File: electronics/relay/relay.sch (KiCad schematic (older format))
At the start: 14 parts, among them J1 Conn_01x01_Female, J2 Conn_01x01_Female, J3 Conn_01x01_Female, J4 Conn_01x01_Female, J5 Conn_01x01_Female, J6 Conn_01x01_Female, J7 Conn_01x01_Female, J8 Conn_01x01_Female, J9 Conn_01x01_Female, K1 SANYOU_SRD_Form_C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

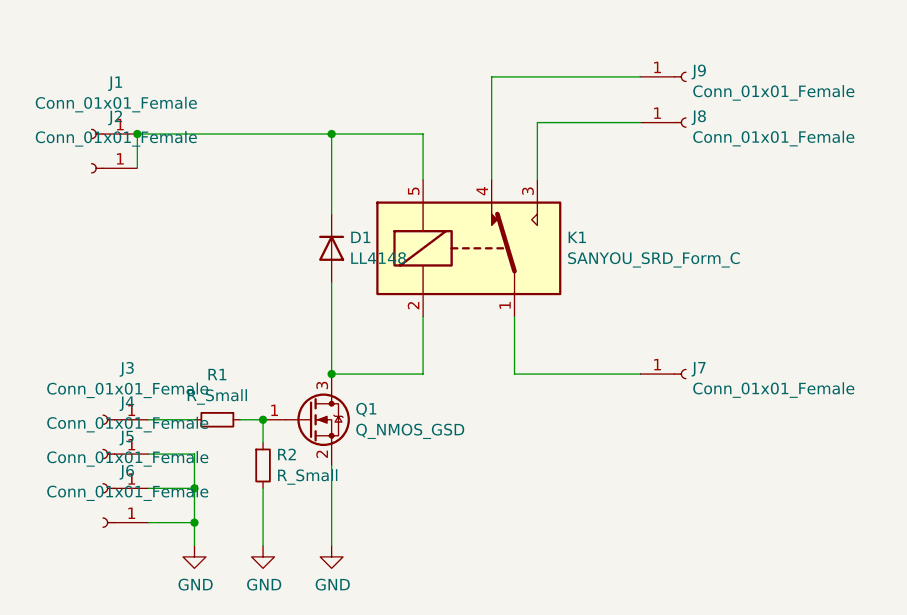
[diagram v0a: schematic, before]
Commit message: Relay board ready, ESP3266 redesign (GPIO16 instead of GPIO0)
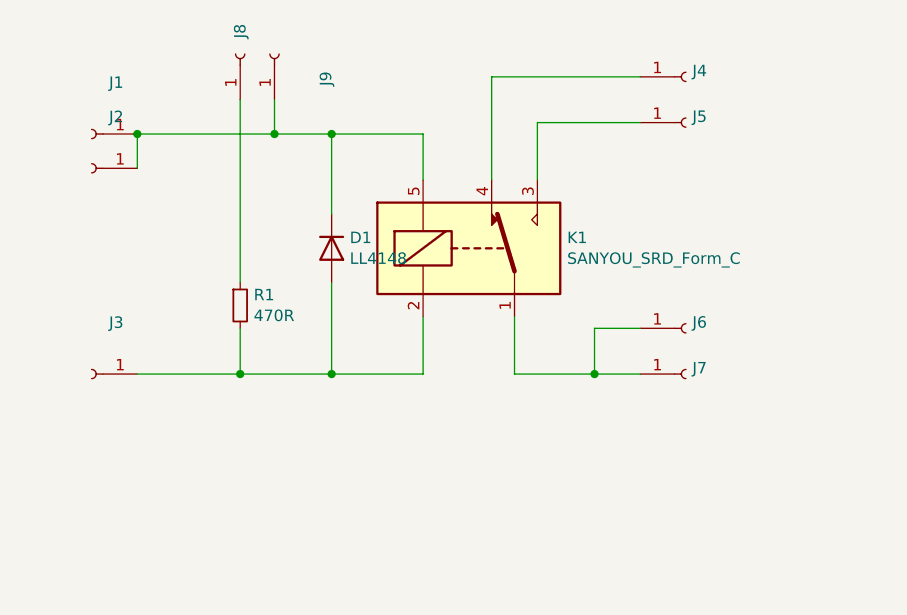
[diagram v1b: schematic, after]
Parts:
- removed J4, J5: Conn_01x01_Female, Connector_Wire:SolderWirePad_1x01_SMD_1x2mm, symbol Connector:Conn_01x01_Female
- removed Q1: Q_NMOS_GSD, Package_TO_SOT_SMD:SOT-23_Handsoldering, symbol Device:Q_NMOS_GSD
- removed R2: R_Small, Resistor_SMD:R_0603_1608Metric_Pad1.05x0.95mm_HandSolder, symbol Device:R_Small
- added J8, J9: Conn_01x01_Female, Connector_Wire:SolderWirePad_1x01_SMD_1x2mm, symbol Connector:Conn_01x01_Female
- D1: footprint Diode_SMD:D_MiniMELF_Handsoldering -> Diode_SMD:D_MiniMELF
- J4: renamed from J9; footprint Connector_Wire:SolderWire-1sqmm_1x01_D1.4mm_OD2.7mm -> Powerstrip:SolderWire-Mains
- J5: renamed from J8; footprint Connector_Wire:SolderWire-1sqmm_1x01_D1.4mm_OD2.7mm -> Powerstrip:SolderWire-Mains
- J6: footprint Connector_Wire:SolderWirePad_1x01_SMD_1x2mm -> Powerstrip:SolderWire-Mains
- J7: footprint Connector_Wire:SolderWire-1sqmm_1x01_D1.4mm_OD2.7mm -> Powerstrip:SolderWire-Mains
- R1: value R_Small -> 470R; footprint Resistor_SMD:R_0603_1608Metric_Pad1.05x0.95mm_HandSolder -> Resistor_SMD:R_0603_1608Metric_Pad0.98x0.95mm_HandSolder
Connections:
- net GND is gone; now on an unnamed net: J6.1 (Pin_1)
- net at D1.2 (A), K1.2: now also J3.1 (Pin_1), R1.2
- net at D1.1 (K), J1.1 (Pin_1), J2.1 (Pin_1)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: now also J9.1 (Pin_1)
- net at R1.1: now also J8.1 (Pin_1)
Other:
- moved on the sheet: J3
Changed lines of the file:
@@
 	1    0    0    -1
-$EndComp
-$Comp
-L Device:Q_NMOS_GSD Q1
-U 1 1 6072ECFD
-P 5450 4900
-F 0 "Q1" H 5654 4946 50  0000 L CNN
-F 1 "Q_NMOS_GSD" H 5654 4855 50  0000 L CNN
-F 2 "Package_TO_SOT_SMD:SOT-23_Handsoldering" H 5650 5000 50  0001 C CNN
-F 3 "~" H 5450 4900 50  0001 C CNN
-	1    5450 4900
-	1    0    0    -1
-$EndComp
-$Comp
-L Device:R_Small R2
-U 1 1 6072F1AD
-P 5250 5100
-F 0 "R2" H 5309 5146 50  0000 L CNN
-F 1 "R_Small" H 5309 5055 50  0000 L CNN
-F 2 "Resistor_SMD:R_0603_1608Metric_Pad1.05x0.95mm_HandSolder" H 5250 5100 50  0001 C CNN
-F 3 "~" H 5250 5100 50  0001 C CNN
-	1    5250 5100
-	1    0    0    -1
-$EndComp
-$Comp
-L Device:R_Small R1
-U 1 1 6072F69D
-P 5050 4900
-F 0 "R1" V 4854 4900 50  0000 C CNN
-F 1 "R_Small" V 4945 4900 50  0000 C CNN
-F 2 "Resistor_SMD:R_0603_1608Metric_Pad1.05x0.95mm_HandSolder" H 5050 4900 50  0001 C CNN
-F 3 "~" H 5050 4900 50  0001 C CNN
-	1    5050 4900
-	0    1    1    0
 $EndComp
 Wire Wire Line
@@
 Wire Wire Line
 	5950 4700 5950 4450
-Wire Wire Line
-	5250 4900 5250 5000
-Wire Wire Line
-	5150 4900 5250 4900
-Connection ~ 5250 4900
-Connection ~ 5550 4700
-$Comp
-L power:GND #PWR02
-U 1 1 60736E18
-P 5250 5450
-F 0 "#PWR02" H 5250 5200 50  0001 C CNN
-F 1 "GND" H 5255 5277 50  0000 C CNN
-F 2 "" H 5250 5450 50  0001 C CNN
-F 3 "" H 5250 5450 50  0001 C CNN
-	1    5250 5450
-	1    0    0    -1
-$EndComp
-$Comp
-L power:GND #PWR01
-U 1 1 60737E22
-P 4950 5450
-F 0 "#PWR01" H 4950 5200 50  0001 C CNN
-F 1 "GND" H 4955 5277 50  0000 C CNN
-F 2 "" H 4950 5450 50  0001 C CNN
-F 3 "" H 4950 5450 50  0001 C CNN
-	1    4950 5450
-	1    0    0    -1
-$EndComp
 $Comp
 L Connector:Conn_01x01_Female J3
 U 1 1 60738ADD
-P 4550 4900
-F 0 "J3" H 4442 4675 50  0000 C CNN
-F 1 "Conn_01x01_Female" H 4442 4766 50  0000 C CNN
-F 2 "Connector_Wire:SolderWirePad_1x01_SMD_1x2mm" H 4550 4900 50  0001 C CNN
-F 3 "~" H 4550 4900 50  0001 C CNN
-	1    4550 4900
-	-1   0    0    1
-$EndComp
-$Comp
-L Connector:Conn_01x01_Female J4
-U 1 1 6073A648
-P 4550 5050
-F 0 "J4" H 4442 4825 50  0000 C CNN
-F 1 "Conn_01x01_Female" H 4442 4916 50  0000 C CNN
-F 2 "Connector_Wire:SolderWirePad_1x01_SMD_1x2mm" H 4550 5050 50  0001 C CNN
-F 3 "~" H 4550 5050 50  0001 C CNN
-	1    4550 5050
+P 4500 4700
+F 0 "J3" H 4392 4475 50  0000 C CNN
+F 1 "Conn_01x01_Female" H 4392 4566 50  0001 C CNN
+F 2 "Connector_Wire:SolderWirePad_1x01_SMD_1x2mm" H 4500 4700 50  0001 C CNN
+F 3 "~" H 4500 4700 50  0001 C CNN
+	1    4500 4700
 	-1   0    0    1
 $EndComp
 Wire Wire Line
-	4750 5050 4950 5050
-Wire Wire Line
-	4950 5050 4950 5200
-Wire Wire Line
-	5250 5200 5250 5450
-Wire Wire Line
-	4750 4900 4950 4900
-$Comp
-L power:GND #PWR03
-U 1 1 6073C2FE
-P 5550 5450
-F 0 "#PWR03" H 5550 5200 50  0001 C CNN
-F 1 "GND" H 5555 5277 50  0000 C CNN
-F 2 "" H 5550 5450 50  0001 C CNN
-F 3 "" H 5550 5450 50  0001 C CNN
-	1    5550 5450
-	1    0    0    -1
-$EndComp
-Wire Wire Line
-	5550 5100 5550 5450
+	4700 4700 5150 4700
 $Comp
 L Connector:Conn_01x01_Female J1
@@
 P 4500 3650
 F 0 "J1" H 4392 3425 50  0000 C CNN
-F 1 "Conn_01x01_Female" H 4392 3516 50  0000 C CNN
+F 1 "Conn_01x01_Female" H 4392 3516 50  0001 C CNN
 F 2 "Connector_Wire:SolderWirePad_1x01_SMD_1x2mm" H 4500 3650 50  0001 C CNN
 F 3 "~" H 4500 3650 50  0001 C CNN
@@
 P 4500 3800
 F 0 "J2" H 4392 3575 50  0000 C CNN
-F 1 "Conn_01x01_Female" H 4392 3666 50  0000 C CNN
+F 1 "Conn_01x01_Female" H 4392 3666 50  0001 C CNN
 F 2 "Connector_Wire:SolderWirePad_1x01_SMD_1x2mm" H 4500 3800 50  0001 C CNN
 F 3 "~" H 4500 3800 50  0001 C CNN
@@
 	-1   0    0    1
 $EndComp
-$Comp
-L Connector:Conn_01x01_Female J5
-U 1 1 6073E6DA
-P 4550 5200
-F 0 "J5" H 4442 4975 50  0000 C CNN
-F 1 "Conn_01x01_Female" H 4442 5066 50  0000 C CNN
-F 2 "Connector_Wire:SolderWirePad_1x01_SMD_1x2mm" H 4550 5200 50  0001 C CNN
-F 3 "~" H 4550 5200 50  0001 C CNN
-	1    4550 5200
-	-1   0    0    1
-$EndComp
-$Comp
-L Connector:Conn_01x01_Female J6
-U 1 1 6073E926
-P 4550 5350
-F 0 "J6" H 4442 5125 50  0000 C CNN
-F 1 "Conn_01x01_Female" H 4442 5216 50  0000 C CNN
-F 2 "Connector_Wire:SolderWirePad_1x01_SMD_1x2mm" H 4550 5350 50  0001 C CNN
-F 3 "~" H 4550 5350 50  0001 C CNN
-	1    4550 5350
-	-1   0    0    1
-$EndComp
-Wire Wire Line
-	4750 5200 4950 5200
-Connection ~ 4950 5200
-Wire Wire Line
-	4950 5200 4950 5350
-Wire Wire Line
-	4750 5350 4950 5350
-Connection ~ 4950 5350
-Wire Wire Line
-	4950 5350 4950 5450
 Wire Wire Line
 	4700 3800 4700 3650
 Wire Wire Line
-	4700 3650 5550 3650
+	4700 3650 5300 3650
 Connection ~ 4700 3650
 Connection ~ 5550 3650
@@
 P 7100 4700
 F 0 "J7" H 7128 4726 50  0000 L CNN
-F 1 "Conn_01x01_Female" H 7128 4635 50  0000 L CNN
-F 2 "Connector_Wire:SolderWire-1sqmm_1x01_D1.4mm_OD2.7mm" H 7100 4700 50  0001 C CNN
+F 1 "Conn_01x01_Female" H 7128 4635 50  0001 L CNN
+F 2 "Powerstrip:SolderWire-Mains" H 7100 4700 50  0001 C CNN
 F 3 "~" H 7100 4700 50  0001 C CNN
 	1    7100 4700
@@
 $EndComp
 $Comp
-L Connector:Conn_01x01_Female J8
+L Connector:Conn_01x01_Female J5
 U 1 1 6074042D
 P 7100 3600
-F 0 "J8" H 7128 3626 50  0000 L CNN
-F 1 "Conn_01x01_Female" H 7128 3535 50  0000 L CNN
-F 2 "Connector_Wire:SolderWire-1sqmm_1x01_D1.4mm_OD2.7mm" H 7100 3600 50  0001 C CNN
+F 0 "J5" H 7128 3626 50  0000 L CNN
+F 1 "Conn_01x01_Female" H 7128 3535 50  0001 L CNN
+F 2 "Powerstrip:SolderWire-Mains" H 7100 3600 50  0001 C CNN
 F 3 "~" H 7100 3600 50  0001 C CNN
 	1    7100 3600
@@
 	6350 4450 6350 4700
 Wire Wire Line
-	6350 4700 6900 4700
+	6350 4700 6700 4700
 $Comp
 L Diode:LL4148 D1
@@
 F 0 "D1" V 5504 4229 50  0000 L CNN
 F 1 "LL4148" V 5595 4229 50  0000 L CNN
-F 2 "Diode_SMD:D_MiniMELF_Handsoldering" H 5550 3975 50  0001 C CNN
+F 2 "Diode_SMD:D_MiniMELF" H 5550 3975 50  0001 C CNN
 F 3 "http://www.vishay.com/docs/85557/ll4148.pdf" H 5550 4150 50  0001 C CNN
 	1    5550 4150
@@
 $EndComp
 $Comp
-L Connector:Conn_01x01_Female J9
+L Connector:Conn_01x01_Female J4
 U 1 1 6074980E
 P 7100 3400
-F 0 "J9" H 7128 3426 50  0000 L CNN
-F 1 "Conn_01x01_Female" H 7128 3335 50  0000 L CNN
-F 2 "Connector_Wire:SolderWire-1sqmm_1x01_D1.4mm_OD2.7mm" H 7100 3400 50  0001 C CNN
+F 0 "J4" H 7128 3426 50  0000 L CNN
+F 1 "Conn_01x01_Female" H 7128 3335 50  0001 L CNN
+F 2 "Powerstrip:SolderWire-Mains" H 7100 3400 50  0001 C CNN
 F 3 "~" H 7100 3400 50  0001 C CNN
 	1    7100 3400
@@
 Wire Wire Line
 	6250 3400 6900 3400
+$Comp
+L Connector:Conn_01x01_Female J6
+U 1 1 60781782
+P 7100 4500
+F 0 "J6" H 7128 4526 50  0000 L CNN
+F 1 "Conn_01x01_Female" H 7128 4435 50  0001 L CNN
+F 2 "Powerstrip:SolderWire-Mains" H 7100 4500 50  0001 C CNN
+F 3 "~" H 7100 4500 50  0001 C CNN
+	1    7100 4500
+	1    0    0    -1
+$EndComp
+Wire Wire Line
+	6900 4500 6700 4500
+Wire Wire Line
+	6700 4500 6700 4700
+Connection ~ 6700 4700
+Wire Wire Line
+	6700 4700 6900 4700
+Connection ~ 5550 4700
+$Comp
+L Device:R_Small R1
+U 1 1 6078AFA8
+P 5150 4400
+F 0 "R1" H 5209 4446 50  0000 L CNN
+F 1 "470R" H 5209 4355 50  0000 L CNN
+F 2 "Resistor_SMD:R_0603_1608Metric_Pad0.98x0.95mm_HandSolder" H 5150 4400 50  0001 C CNN
+F 3 "~" H 5150 4400 50  0001 C CNN
+	1    5150 4400
+	1    0    0    -1
+$EndComp
+Wire Wire Line
+	5150 4500 5150 4700
+Connection ~ 5150 4700
+Wire Wire Line
+	5150 4700 5550 4700
+$Comp
+L Connector:Conn_01x01_Female J8
+U 1 1 6078C226
+P 5150 3300
+F 0 "J8" H 5250 3300 50  0000 C CNN
+F 1 "Conn_01x01_Female" H 5050 3400 50  0001 C CNN
+F 2 "Connector_Wire:SolderWirePad_1x01_SMD_1x2mm" H 5150 3300 50  0001 C CNN
+F 3 "~" H 5150 3300 50  0001 C CNN
+	1    5150 3300
+	0    -1   -1   0
+$EndComp
+$Comp
+L Connector:Conn_01x01_Female J9
+U 1 1 6078C941
+P 5300 3300
+F 0 "J9" H 5192 3075 50  0000 C CNN
+F 1 "Conn_01x01_Female" H 5192 3166 50  0001 C CNN
+F 2 "Connector_Wire:SolderWirePad_1x01_SMD_1x2mm" H 5300 3300 50  0001 C CNN
+F 3 "~" H 5300 3300 50  0001 C CNN
+	1    5300 3300
+	0    -1   -1   0
+$EndComp
+Wire Wire Line
+	5150 4300 5150 3500
+Wire Wire Line
+	5300 3500 5300 3650
+Connection ~ 5300 3650
+Wire Wire Line
+	5300 3650 5550 3650
 $EndSCHEMATC

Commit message: Small PCB modifications, esphome config added
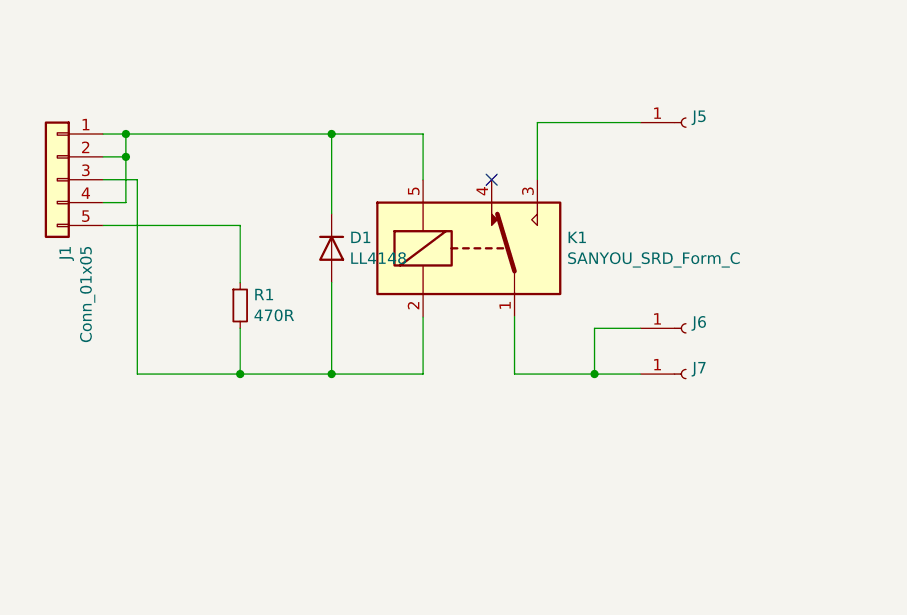
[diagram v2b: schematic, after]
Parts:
- removed J1, J2, J3, J8, J9: Conn_01x01_Female, Connector_Wire:SolderWirePad_1x01_SMD_1x2mm, symbol Connector:Conn_01x01_Female
- removed J4: Conn_01x01_Female, Powerstrip:SolderWire-Mains, symbol Connector:Conn_01x01_Female
- added J1: Conn_01x05, Connector_PinHeader_2.54mm:PinHeader_1x05_P2.54mm_Vertical, symbol Connector_Generic:Conn_01x05
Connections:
- net at D1.2 (A), K1.2, R1.2: now also J1.3 (Pin_3)
- net at D1.1 (K), K1.5: now also J1.1 (Pin_1), J1.2 (Pin_2), J1.4 (Pin_4)
- net at R1.1: now also J1.5 (Pin_5)
- no-connect marks 0 -> 1
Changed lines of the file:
@@
 Wire Wire Line
 	5950 4700 5950 4450
-$Comp
-L Connector:Conn_01x01_Female J3
-U 1 1 60738ADD
-P 4500 4700
-F 0 "J3" H 4392 4475 50  0000 C CNN
-F 1 "Conn_01x01_Female" H 4392 4566 50  0001 C CNN
-F 2 "Connector_Wire:SolderWirePad_1x01_SMD_1x2mm" H 4500 4700 50  0001 C CNN
-F 3 "~" H 4500 4700 50  0001 C CNN
-	1    4500 4700
-	-1   0    0    1
-$EndComp
 Wire Wire Line
 	4700 4700 5150 4700
-$Comp
-L Connector:Conn_01x01_Female J1
-U 1 1 6073DF24
-P 4500 3650
-F 0 "J1" H 4392 3425 50  0000 C CNN
-F 1 "Conn_01x01_Female" H 4392 3516 50  0001 C CNN
-F 2 "Connector_Wire:SolderWirePad_1x01_SMD_1x2mm" H 4500 3650 50  0001 C CNN
-F 3 "~" H 4500 3650 50  0001 C CNN
-	1    4500 3650
-	-1   0    0    1
-$EndComp
-$Comp
-L Connector:Conn_01x01_Female J2
-U 1 1 6073E4C4
-P 4500 3800
-F 0 "J2" H 4392 3575 50  0000 C CNN
-F 1 "Conn_01x01_Female" H 4392 3666 50  0001 C CNN
-F 2 "Connector_Wire:SolderWirePad_1x01_SMD_1x2mm" H 4500 3800 50  0001 C CNN
-F 3 "~" H 4500 3800 50  0001 C CNN
-	1    4500 3800
-	-1   0    0    1
-$EndComp
-Wire Wire Line
-	4700 3800 4700 3650
-Wire Wire Line
-	4700 3650 5300 3650
-Connection ~ 4700 3650
 Connection ~ 5550 3650
-$Comp
-L Connector:Conn_01x01_Female J7
-U 1 1 6073FDB4
-P 7100 4700
-F 0 "J7" H 7128 4726 50  0000 L CNN
-F 1 "Conn_01x01_Female" H 7128 4635 50  0001 L CNN
-F 2 "Powerstrip:SolderWire-Mains" H 7100 4700 50  0001 C CNN
-F 3 "~" H 7100 4700 50  0001 C CNN
-	1    7100 4700
-	1    0    0    -1
-$EndComp
 $Comp
 L Connector:Conn_01x01_Female J5
@@
 	0    1    1    0
 $EndComp
-$Comp
-L Connector:Conn_01x01_Female J4
-U 1 1 6074980E
-P 7100 3400
-F 0 "J4" H 7128 3426 50  0000 L CNN
-F 1 "Conn_01x01_Female" H 7128 3335 50  0001 L CNN
-F 2 "Powerstrip:SolderWire-Mains" H 7100 3400 50  0001 C CNN
-F 3 "~" H 7100 3400 50  0001 C CNN
-	1    7100 3400
-	1    0    0    -1
-$EndComp
-Wire Wire Line
-	6250 3850 6250 3400
-Wire Wire Line
-	6250 3400 6900 3400
-$Comp
-L Connector:Conn_01x01_Female J6
-U 1 1 60781782
-P 7100 4500
-F 0 "J6" H 7128 4526 50  0000 L CNN
-F 1 "Conn_01x01_Female" H 7128 4435 50  0001 L CNN
-F 2 "Powerstrip:SolderWire-Mains" H 7100 4500 50  0001 C CNN
-F 3 "~" H 7100 4500 50  0001 C CNN
-	1    7100 4500
-	1    0    0    -1
-$EndComp
 Wire Wire Line
 	6900 4500 6700 4500
@@
 Wire Wire Line
 	5150 4700 5550 4700
+Wire Wire Line
+	5150 4300 5150 4050
+NoConn ~ 6250 3850
 $Comp
-L Connector:Conn_01x01_Female J8
-U 1 1 6078C226
-P 5150 3300
-F 0 "J8" H 5250 3300 50  0000 C CNN
-F 1 "Conn_01x01_Female" H 5050 3400 50  0001 C CNN
-F 2 "Connector_Wire:SolderWirePad_1x01_SMD_1x2mm" H 5150 3300 50  0001 C CNN
-F 3 "~" H 5150 3300 50  0001 C CNN
-	1    5150 3300
-	0    -1   -1   0
+L Connector_Generic:Conn_01x05 J1
+U 1 1 6094B0FF
+P 4350 3850
+F 0 "J1" V 4314 3562 50  0000 R CNN
+F 1 "Conn_01x05" V 4223 3562 50  0000 R CNN
+F 2 "Connector_PinHeader_2.54mm:PinHeader_1x05_P2.54mm_Vertical" H 4350 3850 50  0001 C CNN
+F 3 "~" H 4350 3850 50  0001 C CNN
+	1    4350 3850
+	-1   0    0    -1
+$EndComp
+Wire Wire Line
+	4550 3650 4650 3650
+Wire Wire Line
+	4650 3650 4650 3750
+Wire Wire Line
+	4650 3750 4550 3750
+Wire Wire Line
+	4650 3750 4650 3950
+Wire Wire Line
+	4650 3950 4550 3950
+Connection ~ 4650 3750
+$Comp
+L Connector:Conn_01x01_Female J6
+U 1 1 60781782
+P 7100 4500
+F 0 "J6" H 7128 4526 50  0000 L CNN
+F 1 "Conn_01x01_Female" H 7128 4435 50  0001 L CNN
+F 2 "Powerstrip:SolderWire-Mains" H 7100 4500 50  0001 C CNN
+F 3 "~" H 7100 4500 50  0001 C CNN
+	1    7100 4500
+	1    0    0    -1
 $EndComp
 $Comp
-L Connector:Conn_01x01_Female J9
-U 1 1 6078C941
-P 5300 3300
-F 0 "J9" H 5192 3075 50  0000 C CNN
-F 1 "Conn_01x01_Female" H 5192 3166 50  0001 C CNN
-F 2 "Connector_Wire:SolderWirePad_1x01_SMD_1x2mm" H 5300 3300 50  0001 C CNN
-F 3 "~" H 5300 3300 50  0001 C CNN
-	1    5300 3300
-	0    -1   -1   0
+L Connector:Conn_01x01_Female J7
+U 1 1 6073FDB4
+P 7100 4700
+F 0 "J7" H 7128 4726 50  0000 L CNN
+F 1 "Conn_01x01_Female" H 7128 4635 50  0001 L CNN
+F 2 "Powerstrip:SolderWire-Mains" H 7100 4700 50  0001 C CNN
+F 3 "~" H 7100 4700 50  0001 C CNN
+	1    7100 4700
+	1    0    0    -1
 $EndComp
+Connection ~ 4650 3650
 Wire Wire Line
-	5150 4300 5150 3500
+	4700 4700 4700 3850
 Wire Wire Line
-	5300 3500 5300 3650
-Connection ~ 5300 3650
+	4700 3850 4550 3850
 Wire Wire Line
-	5300 3650 5550 3650
+	4650 3650 5550 3650
+Wire Wire Line
+	5150 4050 4550 4050
 $EndSCHEMATC
